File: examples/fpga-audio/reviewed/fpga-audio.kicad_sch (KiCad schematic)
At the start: 29 parts, among them J1 3V3 IN, J2 AUDIO OUT, J3 SPI PROG, U1 iCE40UP5K, U2 PCM5102A, U3 AP2112K-1.2, U4 W25Q32JV, X1 12MHz

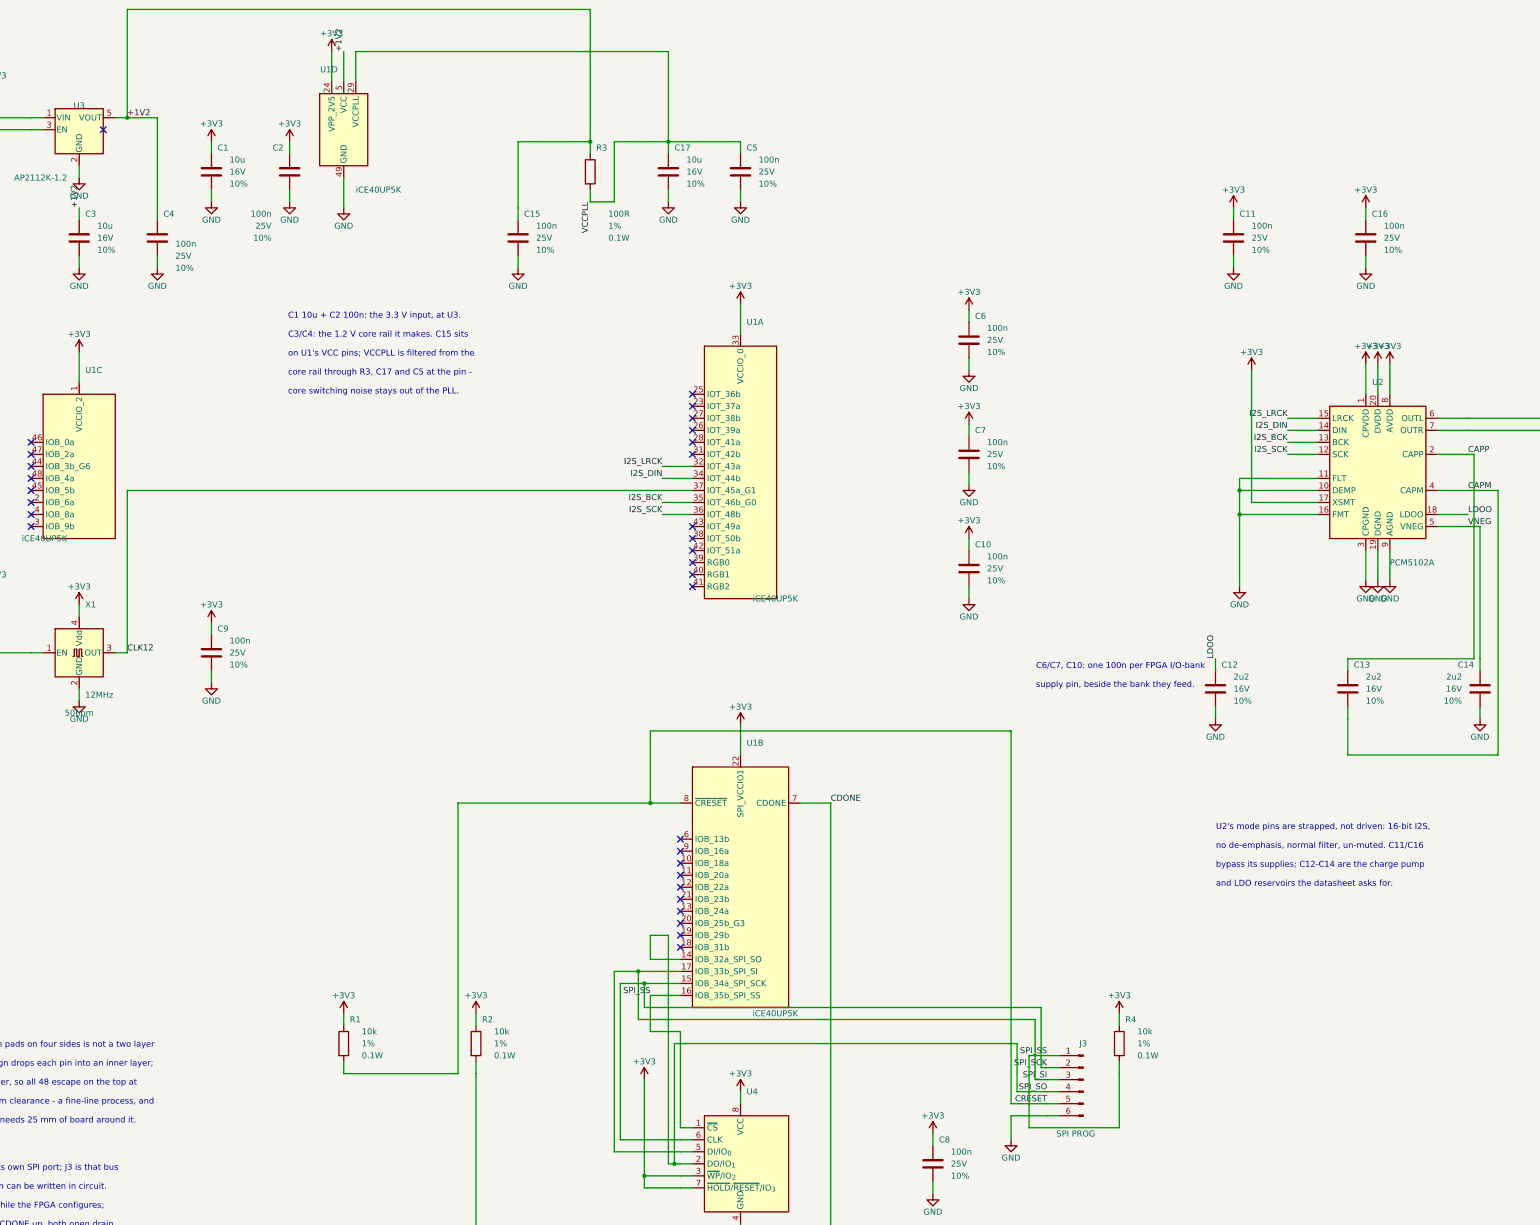
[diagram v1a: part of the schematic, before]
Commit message: Give a turned part's designator somewhere to go
A designator prints horizontally whatever the footprint's rotation, so
on a part turned 90 degrees the string reaches along the axis the
footprint's own frame calls the other one - and a two-terminal chip part
is narrower than its own three-character name. Every spot inside the
footprint touched a pad, and the search gave up and left it there.

It now looks along both local axes, at increasing distance, starting
from half the string plus half the part. Near still beats far.

The fold-back pass also stops refusing to unfold a run that walks back
past where it set out from. That refusal was there because deleting the
point moves the corner before it; usually that corner is the other half
of the same fold and both go. Now it checks: if what is left is 90
degrees or wider, unfold; if not, the run keeps its spur rather than
trade it for a worse bend.
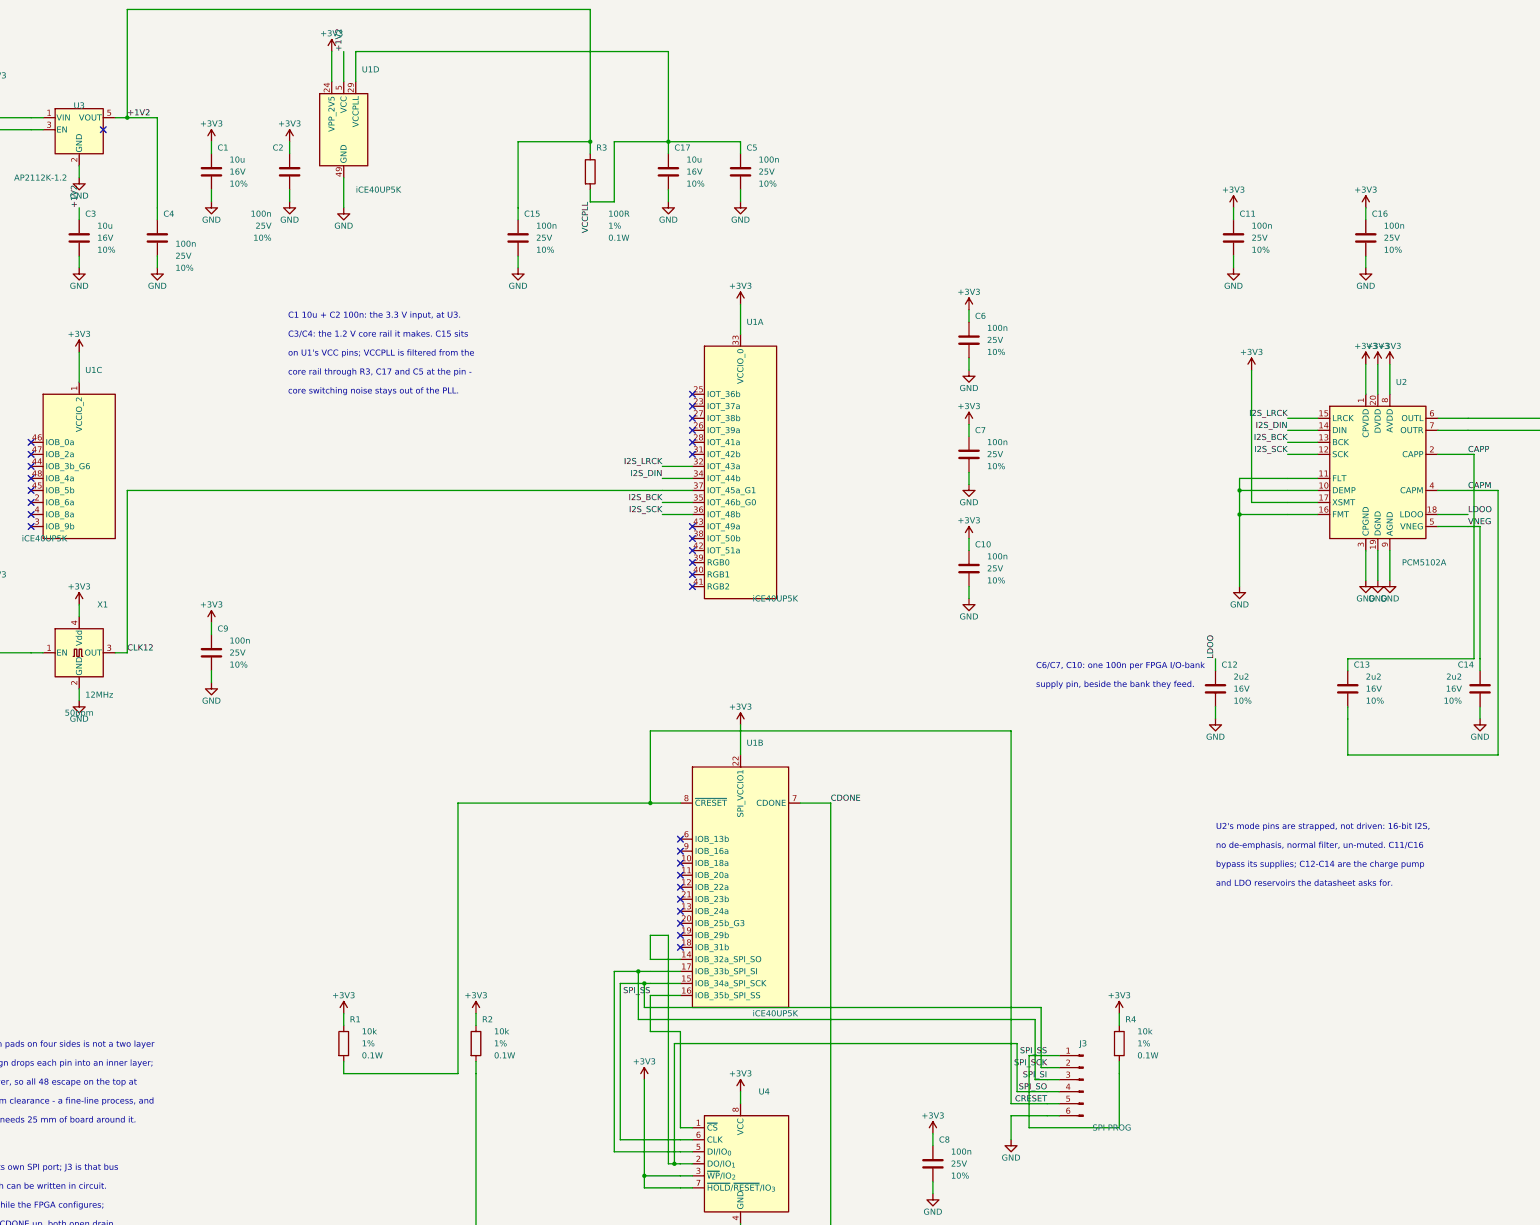
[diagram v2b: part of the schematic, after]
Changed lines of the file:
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@@
   (symbol (lib_id "FPGA_Lattice:ICE40UP5K-SG48ITR") (at 111.76 39.37 0.0) (unit 4)
     (exclude_from_sim no) (in_bom yes) (on_board yes) (dnp no)
-    (property "Reference" "U1" (at 110.49 26.67 0) (effects (font (size 1.27 1.27)) (justify right)))
+    (property "Reference" "U1" (at 115.57 26.67 0) (effects (font (size 1.27 1.27)) (justify left)))
     (property "Value" "iCE40UP5K" (at 114.3 52.07 0) (effects (font (size 1.27 1.27)) (justify left)))
     (property "Footprint" "Package_DFN_QFN:QFN-48-1EP_7x7mm_P0.5mm_EP3.5x3.5mm" (at 111.76 39.37 0) (effects (font (size 1.27 1.27)) hide))
@@
   (symbol (lib_id "Audio:PCM5102A") (at 330.2 110.49 0.0) (unit 1)
     (exclude_from_sim no) (in_bom yes) (on_board yes) (dnp no)
-    (property "Reference" "U2" (at 330.2 92.71 0) (effects (font (size 1.27 1.27))))
-    (property "Value" "PCM5102A" (at 332.74 130.81 0) (effects (font (size 1.27 1.27)) (justify left)))
+    (property "Reference" "U2" (at 334.01 92.71 0) (effects (font (size 1.27 1.27)) (justify left)))
+    (property "Value" "PCM5102A" (at 335.28 130.81 0) (effects (font (size 1.27 1.27)) (justify left)))
     (property "Footprint" "Package_SO:TSSOP-20_4.4x6.5mm_P0.65mm" (at 330.2 110.49 0) (effects (font (size 1.27 1.27)) hide))
     (property "Datasheet" "https://www.ti.com/lit/ds/symlink/pcm5102a.pdf" (at 330.2 110.49 0) (effects (font (size 1.27 1.27)) hide))
@@
   (symbol (lib_id "Memory_Flash:W25Q32JVSS") (at 195.58 257.81 0.0) (unit 1)
     (exclude_from_sim no) (in_bom yes) (on_board yes) (dnp no)
-    (property "Reference" "U4" (at 196.85 242.57 0) (effects (font (size 1.27 1.27)) (justify left)))
+    (property "Reference" "U4" (at 199.39 242.57 0) (effects (font (size 1.27 1.27)) (justify left)))
     (property "Value" "W25Q32JV" (at 198.12 273.05 0) (effects (font (size 1.27 1.27)) (justify left)))
     (property "Footprint" "Package_SO:SOIC-8_3.9x4.9mm_P1.27mm" (at 195.58 257.81 0) (effects (font (size 1.27 1.27)) hide))
@@
   (symbol (lib_id "Oscillator:ASE-xxxMHz") (at 55.88 149.86 0.0) (unit 1)
     (exclude_from_sim no) (in_bom yes) (on_board yes) (dnp no)
-    (property "Reference" "X1" (at 57.15 139.7 0) (effects (font (size 1.27 1.27)) (justify left)))
+    (property "Reference" "X1" (at 59.69 139.7 0) (effects (font (size 1.27 1.27)) (justify left)))
     (property "Value" "12MHz" (at 57.15 158.75 0) (effects (font (size 1.27 1.27)) (justify left)))
     (property "Footprint" "Oscillator:Oscillator_SMD_Abracon_ASE-4Pin_3.2x2.5mm" (at 55.88 149.86 0) (effects (font (size 1.27 1.27)) hide))
@@
     (exclude_from_sim no) (in_bom yes) (on_board yes) (dnp no)
     (property "Reference" "J3" (at 267.97 232.41 0) (effects (font (size 1.27 1.27))))
-    (property "Value" "SPI PROG" (at 270.51 251.46 0) (effects (font (size 1.27 1.27)) (justify left)))
+    (property "Value" "SPI PROG" (at 278.13 250.19 0) (effects (font (size 1.27 1.27)) (justify left)))
     (property "Footprint" "Connector_PinHeader_2.54mm:PinHeader_1x06_P2.54mm_Vertical" (at 267.97 240.03 0) (effects (font (size 1.27 1.27)) hide))
     (property "Datasheet" "https://www.we-online.com/components/products/datasheet/61300611121.pdf" (at 267.97 240.03 0) (effects (font (size 1.27 1.27)) hide))
